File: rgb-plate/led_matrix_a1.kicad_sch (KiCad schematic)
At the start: 64 parts

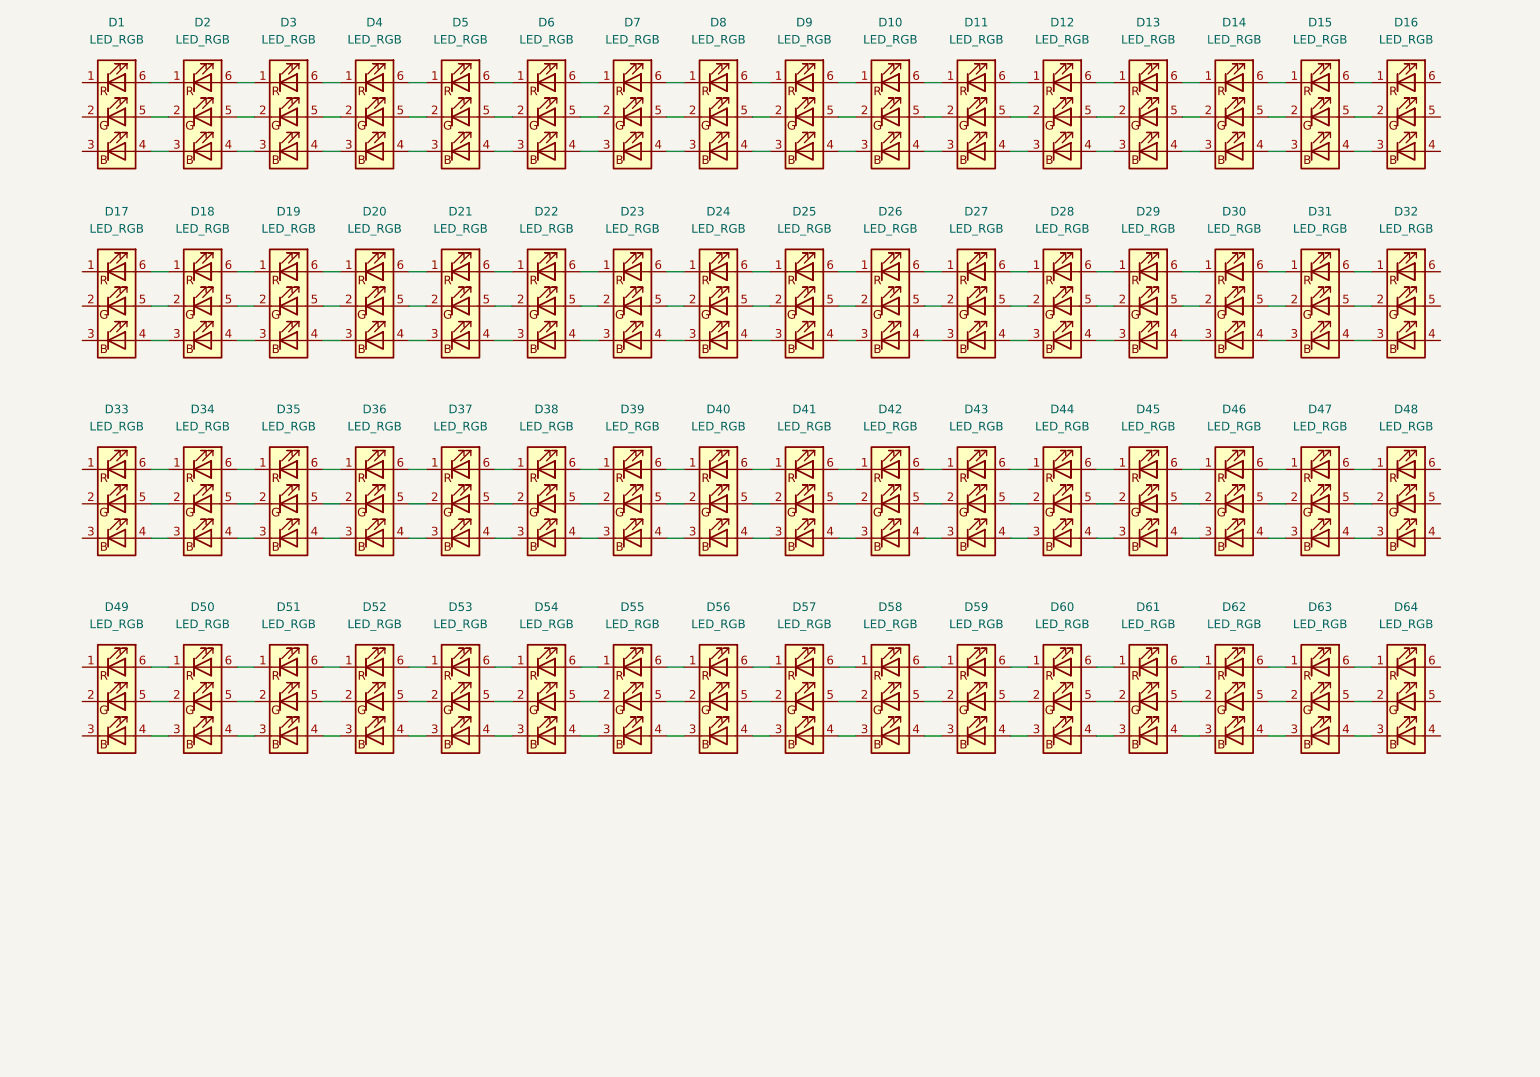
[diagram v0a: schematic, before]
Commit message: initial layout on single board, may need to split up
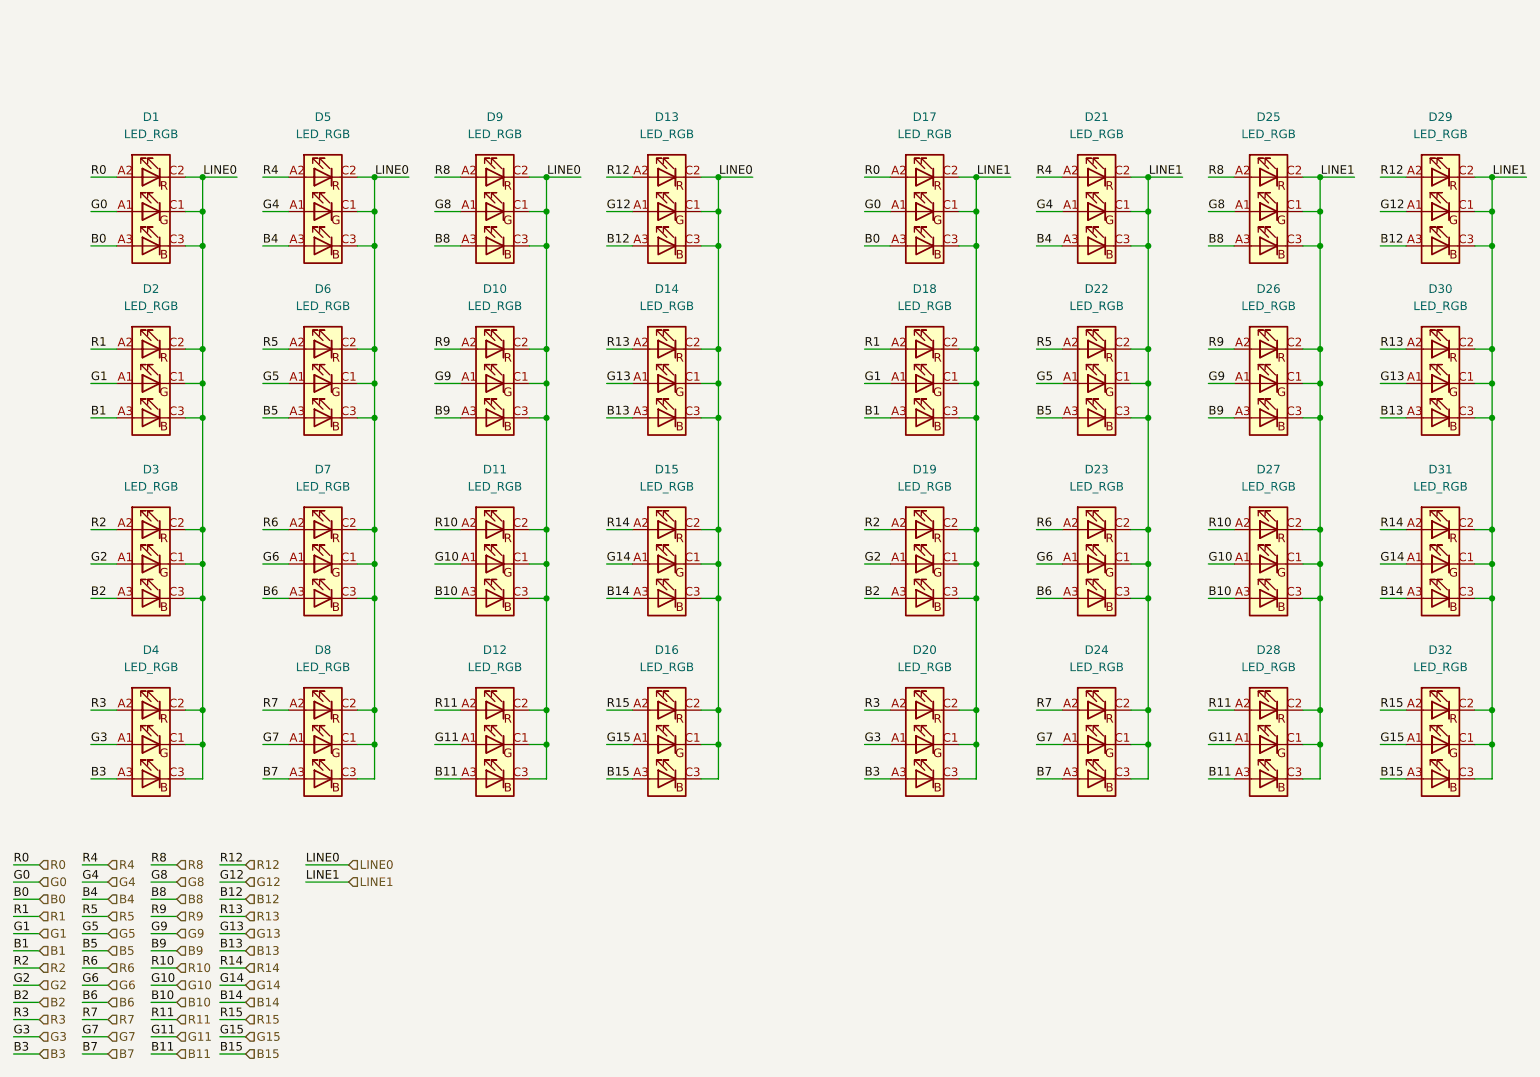
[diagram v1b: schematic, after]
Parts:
- removed D10, D11, D12, D13, D14, D15, D16, D17, D18, D19, D20, D21, D22, D23, D24, D25, D26, D27, D28, D29, D30, D31, D32, D33, D34, D35, D36, D37, D38, D39, D40, D41, D42, D43, D44, D45, D46, D47, D48, D49, D5, D50, D51, D52, D53, D54, D55, D56, D57, D58, D59, D6, D60, D61, D62, D63, D64, D7, D8, D9: LED_RGB, symbol Device:LED_RGB
- added D10, D11, D12, D13, D14, D15, D16, D17, D18, D19, D20, D21, D22, D23, D24, D25, D26, D27, D28, D29, D30, D31, D32, D5, D6, D7, D8, D9: LED_RGB, LRTBGVSR-4U4V-JW+8A8B-D8-3S4U-7Z:LRTBGVSR4U4VJW8A8BD83S4U7Z, symbol LRTBGVSR-4U4V-JW+8A8B-D8-3S4U-:LED_RGB
- D1, D2, D3, D4: footprint (none) -> LRTBGVSR-4U4V-JW+8A8B-D8-3S4U-7Z:LRTBGVSR4U4VJW8A8BD83S4U7Z; symbol Device:LED_RGB -> LRTBGVSR-4U4V-JW+8A8B-D8-3S4U-:LED_RGB
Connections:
- new net B0: D1.A3 (BA), D17.A3 (BA)
- new net B1: D18.A3 (BA), D2.A3 (BA)
- new net B10: D11.A3 (BA), D27.A3 (BA)
- new net B11: D12.A3 (BA), D28.A3 (BA)
- new net B12: D13.A3 (BA), D29.A3 (BA)
- new net B13: D14.A3 (BA), D30.A3 (BA)
- new net B14: D15.A3 (BA), D31.A3 (BA)
- new net B15: D16.A3 (BA), D32.A3 (BA)
- new net B2: D19.A3 (BA), D3.A3 (BA)
- new net B3: D20.A3 (BA), D4.A3 (BA)
- new net B4: D21.A3 (BA), D5.A3 (BA)
- new net B5: D22.A3 (BA), D6.A3 (BA)
- new net B6: D23.A3 (BA), D7.A3 (BA)
- new net B7: D24.A3 (BA), D8.A3 (BA)
- new net B8: D25.A3 (BA), D9.A3 (BA)
- new net B9: D10.A3 (BA), D26.A3 (BA)
- new net G0: D1.A1 (GA), D17.A1 (GA)
- new net G1: D18.A1 (GA), D2.A1 (GA)
- new net G10: D11.A1 (GA), D27.A1 (GA)
- new net G11: D12.A1 (GA), D28.A1 (GA)
- new net G12: D13.A1 (GA), D29.A1 (GA)
- new net G13: D14.A1 (GA), D30.A1 (GA)
- new net G14: D15.A1 (GA), D31.A1 (GA)
- new net G15: D16.A1 (GA), D32.A1 (GA)
- new net G2: D19.A1 (GA), D3.A1 (GA)
- new net G3: D20.A1 (GA), D4.A1 (GA)
- new net G4: D21.A1 (GA), D5.A1 (GA)
- new net G5: D22.A1 (GA), D6.A1 (GA)
- new net G6: D23.A1 (GA), D7.A1 (GA)
- new net G7: D24.A1 (GA), D8.A1 (GA)
- new net G8: D25.A1 (GA), D9.A1 (GA)
- new net G9: D10.A1 (GA), D26.A1 (GA)
- new net LINE0: D1.C1 (GK), D1.C2 (RK), D1.C3 (BK), D10.C1 (GK), D10.C2 (RK), D10.C3 (BK), D11.C1 (GK), D11.C2 (RK), D11.C3 (BK), D12.C1 (GK), D12.C2 (RK), D12.C3 (BK), D13.C1 (GK), D13.C2 (RK), D13.C3 (BK), D14.C1 (GK), D14.C2 (RK), D14.C3 (BK), D15.C1 (GK), D15.C2 (RK), D15.C3 (BK), D16.C1 (GK), D16.C2 (RK), D16.C3 (BK), D2.C1 (GK), D2.C2 (RK), D2.C3 (BK), D3.C1 (GK), D3.C2 (RK), D3.C3 (BK), D4.C1 (GK), D4.C2 (RK), D4.C3 (BK), D5.C1 (GK), D5.C2 (RK), D5.C3 (BK), D6.C1 (GK), D6.C2 (RK), D6.C3 (BK), D7.C1 (GK), D7.C2 (RK), D7.C3 (BK), D8.C1 (GK), D8.C2 (RK), D8.C3 (BK), D9.C1 (GK), D9.C2 (RK), D9.C3 (BK)
- new net LINE1: D17.C1 (GK), D17.C2 (RK), D17.C3 (BK), D18.C1 (GK), D18.C2 (RK), D18.C3 (BK), D19.C1 (GK), D19.C2 (RK), D19.C3 (BK), D20.C1 (GK), D20.C2 (RK), D20.C3 (BK), D21.C1 (GK), D21.C2 (RK), D21.C3 (BK), D22.C1 (GK), D22.C2 (RK), D22.C3 (BK), D23.C1 (GK), D23.C2 (RK), D23.C3 (BK), D24.C1 (GK), D24.C2 (RK), D24.C3 (BK), D25.C1 (GK), D25.C2 (RK), D25.C3 (BK), D26.C1 (GK), D26.C2 (RK), D26.C3 (BK), D27.C1 (GK), D27.C2 (RK), D27.C3 (BK), D28.C1 (GK), D28.C2 (RK), D28.C3 (BK), D29.C1 (GK), D29.C2 (RK), D29.C3 (BK), D30.C1 (GK), D30.C2 (RK), D30.C3 (BK), D31.C1 (GK), D31.C2 (RK), D31.C3 (BK), D32.C1 (GK), D32.C2 (RK), D32.C3 (BK)
- new net R0: D1.A2 (RA), D17.A2 (RA)
- new net R1: D18.A2 (RA), D2.A2 (RA)
- new net R10: D11.A2 (RA), D27.A2 (RA)
- new net R11: D12.A2 (RA), D28.A2 (RA)
- new net R12: D13.A2 (RA), D29.A2 (RA)
- new net R13: D14.A2 (RA), D30.A2 (RA)
- new net R14: D15.A2 (RA), D31.A2 (RA)
- new net R15: D16.A2 (RA), D32.A2 (RA)
- new net R2: D19.A2 (RA), D3.A2 (RA)
- new net R3: D20.A2 (RA), D4.A2 (RA)
- new net R4: D21.A2 (RA), D5.A2 (RA)
- new net R5: D22.A2 (RA), D6.A2 (RA)
- new net R6: D23.A2 (RA), D7.A2 (RA)
- new net R7: D24.A2 (RA), D8.A2 (RA)
- new net R8: D25.A2 (RA), D9.A2 (RA)
- new net R9: D10.A2 (RA), D26.A2 (RA)
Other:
- moved on the sheet: D1, D2, D3, D4
